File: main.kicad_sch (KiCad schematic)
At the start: 15 parts, among them J1 Conn_02x16_Row_Letter_First

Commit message: Updated documentation
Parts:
- TP4, TP5, TP6: DNP (none) -> 1; Note (none) -> Solder only for debugging
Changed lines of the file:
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@@
+      (effects (font (size 1.27 1.27)) hide)
+    )
+    (property "DNP" "1" (id 6) (at 77.47 53.34 0)
+      (effects (font (size 1.27 1.27)) hide)
+    )
+    (property "Note" "Solder only for debugging" (id 7) (at 77.47 53.34 0)
       (effects (font (size 1.27 1.27)) hide)
     )
@@
       (effects (font (size 1.27 1.27)) hide)
     )
+    (property "DNP" "1" (id 6) (at 90.17 53.34 0)
+      (effects (font (size 1.27 1.27)) hide)
+    )
+    (property "Note" "Solder only for debugging" (id 7) (at 90.17 53.34 0)
+      (effects (font (size 1.27 1.27)) hide)
+    )
     (pin "1")
   )
@@
       (effects (font (size 1.27 1.27)) hide)
     )
+    (property "DNP" "1" (id 6) (at 102.87 53.34 0)
+      (effects (font (size 1.27 1.27)) hide)
+    )
+    (property "Note" "Solder only for debugging" (id 7) (at 102.87 53.34 0)
+      (effects (font (size 1.27 1.27)) hide)
+    )

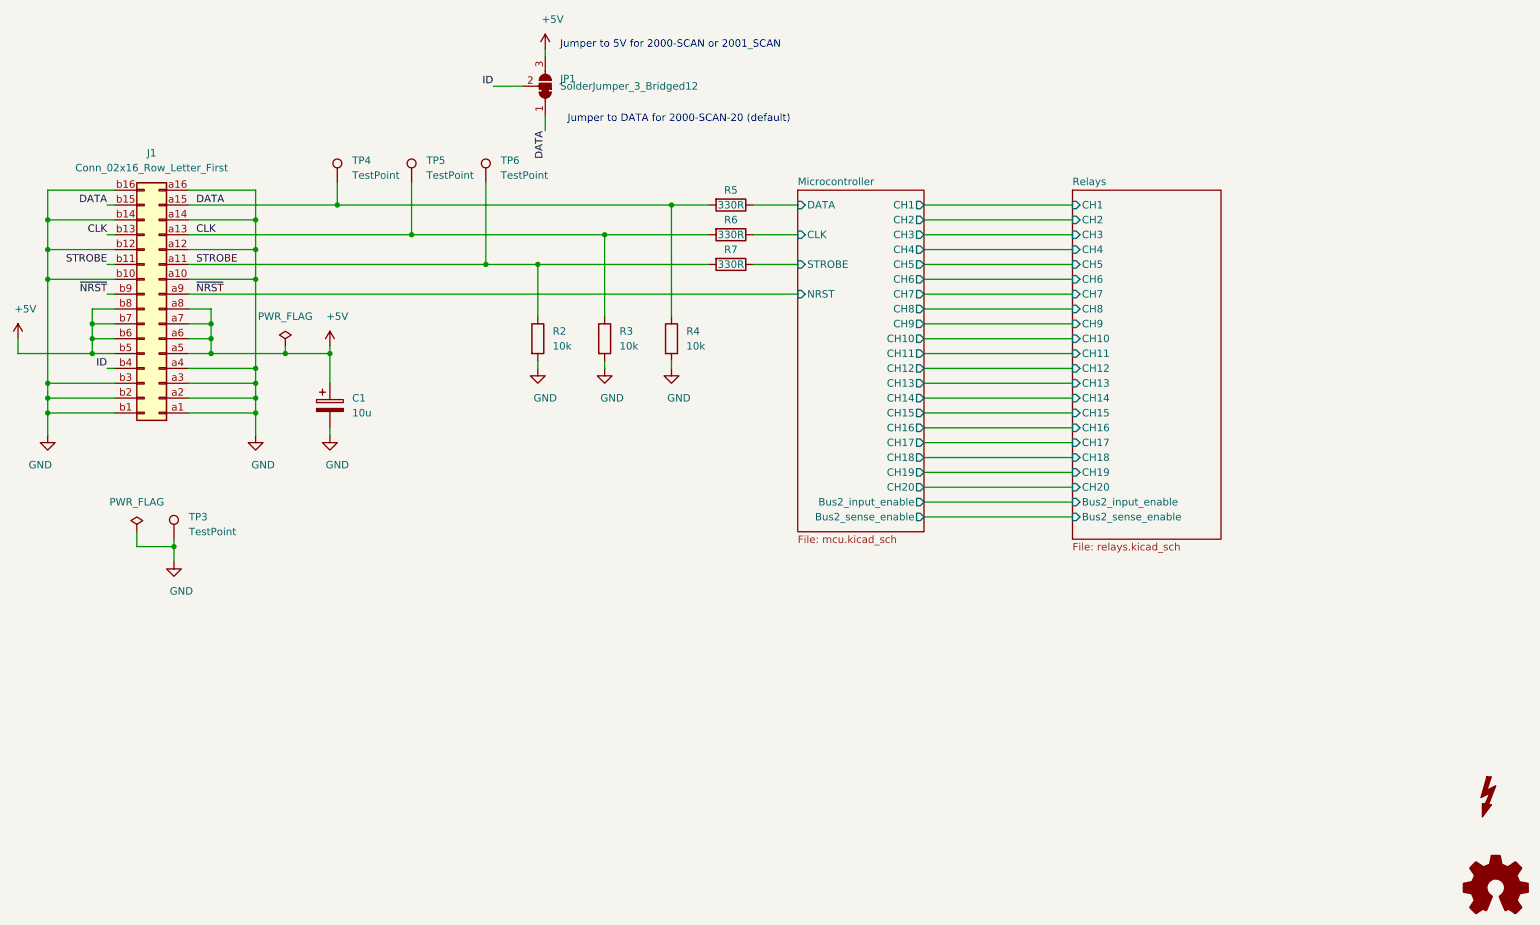
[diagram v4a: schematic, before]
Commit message: Updated to KiCad 8 (#1)
- Updated libraries
- Updated BOM, replaced obsolete parts
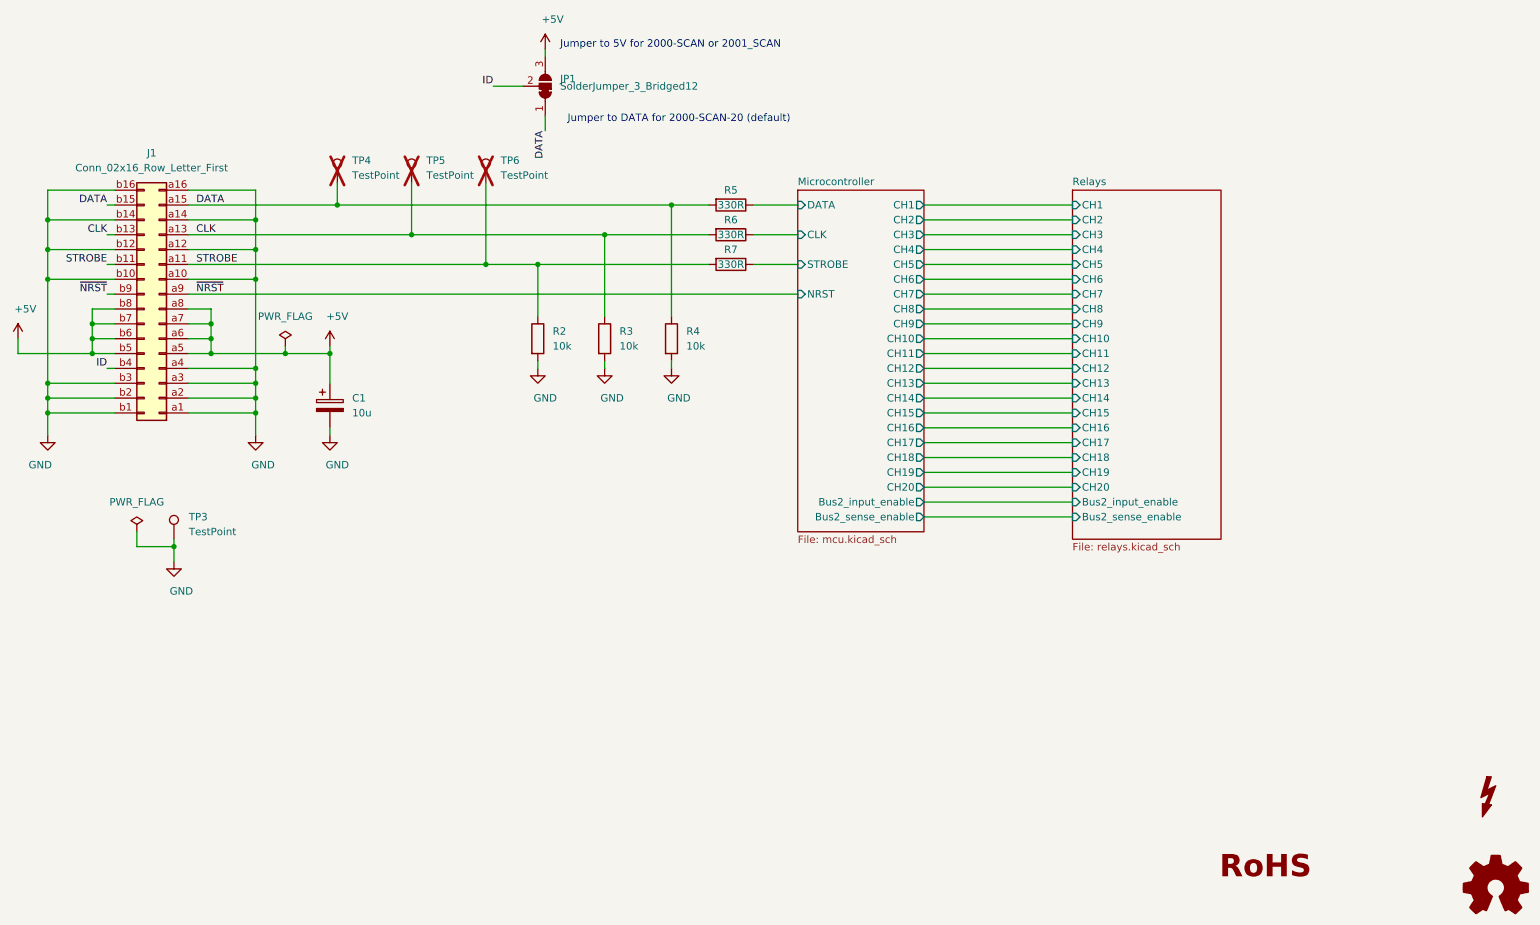
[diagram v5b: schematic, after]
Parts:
- C1: MFN Nichicon -> Rubycon; PN ULD2A100MED1TD -> 100YXM10MEFR6; RoHS (none) -> Yes; Temperature (none) -> Tstorage = –40 °C to 105 °C
- J1: RoHS (none) -> Yes; Temperature (none) -> Tstorage = –55 °C to 125 °C
- R2, R3, R4, R5, R6, R7: RoHS (none) -> By exemption; Temperature (none) -> Tstorage = –55 °C to 155 °C
- SYM1: footprint Symbol:Symbol_Highvoltage_Type2_CopperTop_Small -> Symbol:Symbol_HighVoltage_Triangle_17x15mm_Copper
- TP3: RoHS (none) -> Yes
- TP4, TP5, TP6: DNP 1 -> (none); RoHS (none) -> Yes; now not fitted
